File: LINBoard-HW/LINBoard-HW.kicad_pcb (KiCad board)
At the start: 2 copper layers, 77 parts, among them J1 DEBUG, J2 USB_C_Receptacle_USB2.0, SW2 RESET, SW3 BOOT, U1 RP2350_60QFN, U2 TJA1029T, U3 TPS56339DDC, U4 LD1117S33CTR, U5 W25Q128JVS, U6 MCP25625x-x-ML, Y1 ABM8-272-T3

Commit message: board layout started
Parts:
- removed C18: 1uF, Capacitor_SMD:C_0603_1608Metric
- added D1: PESD1LIN, Diode_SMD:D_SOD-323, F.Cu at (0.00, 3.81)
- added D14: Schottky, Diode_SMD:D_SOD-123, F.Cu at (12.3, 31.0)
- added D2: Schottky, Diode_SMD:D_SOD-123, F.Cu at (0.25, -1.52)
- added D3: Schottky, Diode_SMD:D_SOD-123, F.Cu at (9.91, -4.32)
- added J4: ATM15-6P-BM03, ATM:ATM13-6P, F.Cu at (0.00, -23.3)
- added JP6: MASTER, Jumper:SolderJumper-2_P1.3mm_Bridged_RoundedPad1.0x1.5mm, F.Cu at (0.00, 1.27)
- added L2: 5.6uH, Inductors_SMD:Wuerth_LHMI, F.Cu at (12.4, 1.52)
- added Y2: 16MHz 12pF, Crystal:Crystal_SMD_3225-4Pin_3.2x2.5mm, F.Cu at (-12.3, 7.28)
- C1, C10, C11, C12, C13, C14, C15, C16, C17, C19, C2, C22, C23, C24, C25, C26, C27, C28, C29, C3, C30, C31, C4, C5, C6, C7, C8, C9: footprint Capacitor_SMD:C_0603_1608Metric -> Capacitor_SMD:C_0402_1005Metric
- C20, C21: footprint Capacitor_SMD:C_0603_1608Metric -> RP2350_60QFN_minimal:C_0402_1005Metric_small_pads
- D5, D6, D8, D9: footprint LED_SMD:LED_0805_2012Metric -> LED_SMD:LED_0603_1608Metric
- R1, R10, R11, R12, R13, R14, R15, R16, R17, R18, R19, R2, R20, R21, R22, R23, R24, R3, R4, R5, R6, R7, R8, R9: footprint Resistor_SMD:R_0603_1608Metric -> Resistor_SMD:R_0402_1005Metric
- SW2, SW3: footprint Button_Switch_SMD:SW_Push_1P1T_NO_Vertical_Wuerth_434133025816 -> Buttons:TS-1088-AR02016
- moved D5 51.0 mm to (-8.38, 38.4), turned to 180 degrees
- moved U6 50.4 mm to (-10.1, 15.1), turned to 90 degrees
- moved C31 48.6 mm to (-11.7, -5.08)
- moved R1 48.5 mm to (2.29, 1.27), turned to -90 degrees
- moved R4 48.5 mm to (-14.5, 18.8), turned to 90 degrees
- moved C30 47.9 mm to (-15.5, -5.08), turned to 180 degrees
- moved D6 47.7 mm to (-7.11, -3.84), turned to -90 degrees
- moved C2 47.5 mm to (-2.54, 4.83), turned to 90 degrees
- moved U2 47.3 mm to (-0.51, 10.2), turned to 90 degrees
- moved R2 47.3 mm to (-4.06, 11.9), turned to -90 degrees
- moved C5 46.6 mm to (-13.5, 9.91), turned to 180 degrees
- moved U4 46.1 mm to (-12.2, 0.00), turned to 180 degrees
- moved D8 45.7 mm to (-3.81, 38.4)
- moved R18 45.3 mm to (-11.9, 19.6)
- moved R24 45.1 mm to (-7.11, -1.52)
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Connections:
- net Net-(U3-SW) renamed /Power/SW
- C24 pad 1: Net-(D3-K) -> +12P
- C25 pad 1: Net-(D3-K) -> +12P
- C26 pad 1: Net-(D3-K) -> +12P
- J1 pad MP: (no net) -> GND
- R2 pad 1: +12P -> +3.3V
- U1 pad 13: /Connectors/ENABLE -> unconnected-(U1-GPIO9-Pad13)
- U3 pad 3: Net-(D3-K) -> +12P
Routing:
- net +5V: track 0.00 -> 65.7 mm, vias 0 -> 7
- net +3.3V: track 0.00 -> 59.8 mm, vias 0 -> 13
- net CAN_H: track 0.00 -> 33.6 mm
- net CAN_L: track 0.00 -> 26.9 mm
- net GND: track 0.00 -> 24.5 mm, vias 0 -> 22
- net /Microcontroller/QSPI_SS: track 0.00 -> 24.5 mm
- net +12P: track 0.00 -> 23.1 mm
- net +1V1: track 0.00 -> 22.7 mm, vias 0 -> 9
- net /CAN/~{INT}: track 0.00 -> 22.3 mm, vias 0 -> 2
- net /CAN/~{RX0BF}: track 0.00 -> 22.2 mm, vias 0 -> 2
- net /CAN/SCK: track 0.00 -> 17.3 mm, vias 0 -> 2
- net /Microcontroller/QSPI_SD1: track 0.00 -> 16.5 mm
- net /Microcontroller/RUN: track 0.00 -> 16.4 mm
- net /LIN/RX: track 0.00 -> 15.6 mm
- net /CAN/MOSI: track 0.00 -> 15.6 mm, vias 0 -> 2
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- added copper zone on F.Cu, net +12P
- added copper zone on F.Cu, net +12V
- added copper zone on F.Cu, net +1V1
- added copper zone on F.Cu, net +3.3V
- added copper zone on In1.Cu, net +3.3V
- added copper zone on F.Cu, net +5V
- added copper zone on F.Cu, net /Microcontroller/VREG_LX
- added copper zone on F.Cu, net /Power/SW
- added copper zone on B.Cu, net GND
- added copper zone on F.Cu, net GND
- added copper zone on In2.Cu, net GND
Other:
- board outline added: 34.4 x 68.5 mm
- copper layers 2 -> 4
- board text added: "BOOT"
- board text added: "CAN"
- board text added: "LIN"
- board text added: "RUN"
- board text added: "STS"

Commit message: moving some things around
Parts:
- moved D14 4.04 mm to (15.2, 28.2), turned to -90 degrees
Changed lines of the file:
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@@
 	(footprint "Diode_SMD:D_SOD-123"
 		(layer "F.Cu")
-		(at 12.318 30.988 180)
+		(at 15.24 28.194 -90)
 		(descr "SOD-123")
 		(tags "SOD-123")
 		(property "Reference" "D14"
-			(at -74.646 -30.194 0)
+			(at -74.646 -30.194 90)
 			(layer "F.SilkS")
 			(hide yes)
@@
 		)
 		(property "Value" "Schottky"
-			(at 0 2.1 0)
+			(at 0 2.1 90)
 			(layer "F.Fab")
 			(effects
@@
 		)
 		(property "Datasheet" "~"
-			(at 0 0 180)
+			(at 0 0 270)
 			(unlocked yes)
 			(layer "F.Fab")
@@
 		)
 		(property "Description" "Schottky diode, small symbol, filled shape"
-			(at 0 0 180)
+			(at 0 0 270)
 			(unlocked yes)
 			(layer "F.Fab")
@@
 		(fp_line
 			(start -2.36 -1)
-			(end 1.65 -1)
+			(end -2.36 1)
 			(stroke
 				(width 0.12)
@@
 		(fp_line
 			(start -2.36 -1)
-			(end -2.36 1)
+			(end 1.65 -1)
 			(stroke
 				(width 0.12)
@@
 		)
 		(fp_line
-			(start 2.35 -1.15)
-			(end 2.35 1.15)
+			(start -2.35 -1.15)
+			(end -2.35 1.15)
 			(stroke
 				(width 0.05)
@@
 		)
 		(fp_line
-			(start -2.35 -1.15)
-			(end -2.35 1.15)
+			(start 2.35 -1.15)
+			(end 2.35 1.15)
 			(stroke
 				(width 0.05)
@@
 		)
 		(fp_line
-			(start 1.4 0.9)
-			(end -1.4 0.9)
+			(start -1.4 0.9)
+			(end -1.4 -0.9)
 			(stroke
 				(width 0.1)
@@
 		)
 		(fp_line
-			(start 1.4 -0.9)
-			(end 1.4 0.9)
+			(start 1.4 0.9)
+			(end -1.4 0.9)
 			(stroke
 				(width 0.1)
@@
 		)
 		(fp_line
-			(start 0.25 0)
-			(end 0.75 0)
+			(start -0.75 0)
+			(end -0.35 0)
 			(stroke
 				(width 0.1)
@@
 		)
 		(fp_line
-			(start 0.25 -0.4)
-			(end 0.25 0.4)
+			(start -0.35 0)
+			(end -0.35 0.55)
 			(stroke
 				(width 0.1)
@@
 		(fp_line
 			(start -0.35 0)
-			(end -0.35 0.55)
+			(end -0.35 -0.55)
 			(stroke
 				(width 0.1)
@@
 		)
 		(fp_line
-			(start -0.35 0)
-			(end -0.35 -0.55)
+			(start 0.25 0)
+			(end 0.75 0)
 			(stroke
 				(width 0.1)
@@
 		)
 		(fp_line
-			(start -0.75 0)
-			(end -0.35 0)
+			(start 0.25 -0.4)
+			(end 0.25 0.4)
 			(stroke
 				(width 0.1)
@@
 		)
 		(fp_line
-			(start -1.4 0.9)
-			(end -1.4 -0.9)
+			(start -1.4 -0.9)
+			(end 1.4 -0.9)
 			(stroke
 				(width 0.1)
@@
 		)
 		(fp_line
-			(start -1.4 -0.9)
-			(end 1.4 -0.9)
+			(start 1.4 -0.9)
+			(end 1.4 0.9)
 			(stroke
 				(width 0.1)
@@
 		)
 		(fp_text user "${REFERENCE}"
-			(at 0 -2 0)
+			(at 0 -2 90)
 			(layer "F.Fab")
 			(effects
@@
 		)
 		(pad "1" smd roundrect
-			(at -1.65 0 180)
+			(at -1.65 0 270)
 			(size 0.9 1.2)
 			(layers "F.Cu" "F.Mask" "F.Paste")
@@
 		)
 		(pad "2" smd roundrect
-			(at 1.65 0 180)
+			(at 1.65 0 270)
 			(size 0.9 1.2)
 			(layers "F.Cu" "F.Mask" "F.Paste")
@@
 	)
 	(segment
-		(start -14.506 -3.15)
-		(end -14.506 4.302)
+		(start -13.728 5.08)
+		(end -10.414 5.08)
 		(width 0.15)
 		(layer "F.Cu")
@@
 	)
 	(segment
-		(start -14.506 4.302)
-		(end -13.728 5.08)
+		(start -14.506 -3.15)
+		(end -14.506 4.302)
 		(width 0.15)
 		(layer "F.Cu")
@@
 	)
 	(segment
-		(start -11.071906 5.08)
-		(end -9.652 6.499906)
+		(start -10.414 5.08)
+		(end -9.652 5.842)
 		(width 0.15)
 		(layer "F.Cu")
@@
 	)
 	(segment
-		(start -9.172 9.116)
+		(start -8.636 9.670001)
 		(end -8.636 9.116)
 		(width 0.15)
@@
 	)
 	(segment
-		(start -8.636 9.670001)
-		(end -8.636 9.116)
+		(start -10.706 12.2525)
+		(end -10.706 11.740001)
 		(width 0.15)
 		(layer "F.Cu")
@@
 	)
 	(segment
-		(start -9.652 6.499906)
-		(end -9.652 8.636)
+		(start -9.172 9.116)
+		(end -8.636 9.116)
 		(width 0.15)
 		(layer "F.Cu")
@@
 	)
 	(segment
-		(start -10.706 12.2525)
-		(end -10.706 11.740001)
-		(width 0.15)
+		(start -14.506 -5.56)
+		(end -14.478 -5.588)
+		(width 1.5)
 		(layer "F.Cu")
 		(net 4)
 	)
 	(segment
-		(start -14.506 -5.56)
-		(end -14.478 -5.588)
+		(start -14.506 -3.15)
+		(end -14.506 -5.56)
 		(width 1.5)
 		(layer "F.Cu")
@@
 	)
 	(segment
-		(start -13.728 5.08)
-		(end -11.071906 5.08)
+		(start -9.652 5.842)
+		(end -9.652 8.636)
 		(width 0.15)
 		(layer "F.Cu")
@@
 	)
 	(segment
-		(start -14.506 -3.15)
-		(end -14.506 -5.56)
-		(width 1.5)
+		(start -14.506 4.302)
+		(end -13.728 5.08)
+		(width 0.15)
 		(layer "F.Cu")
 		(net 4)

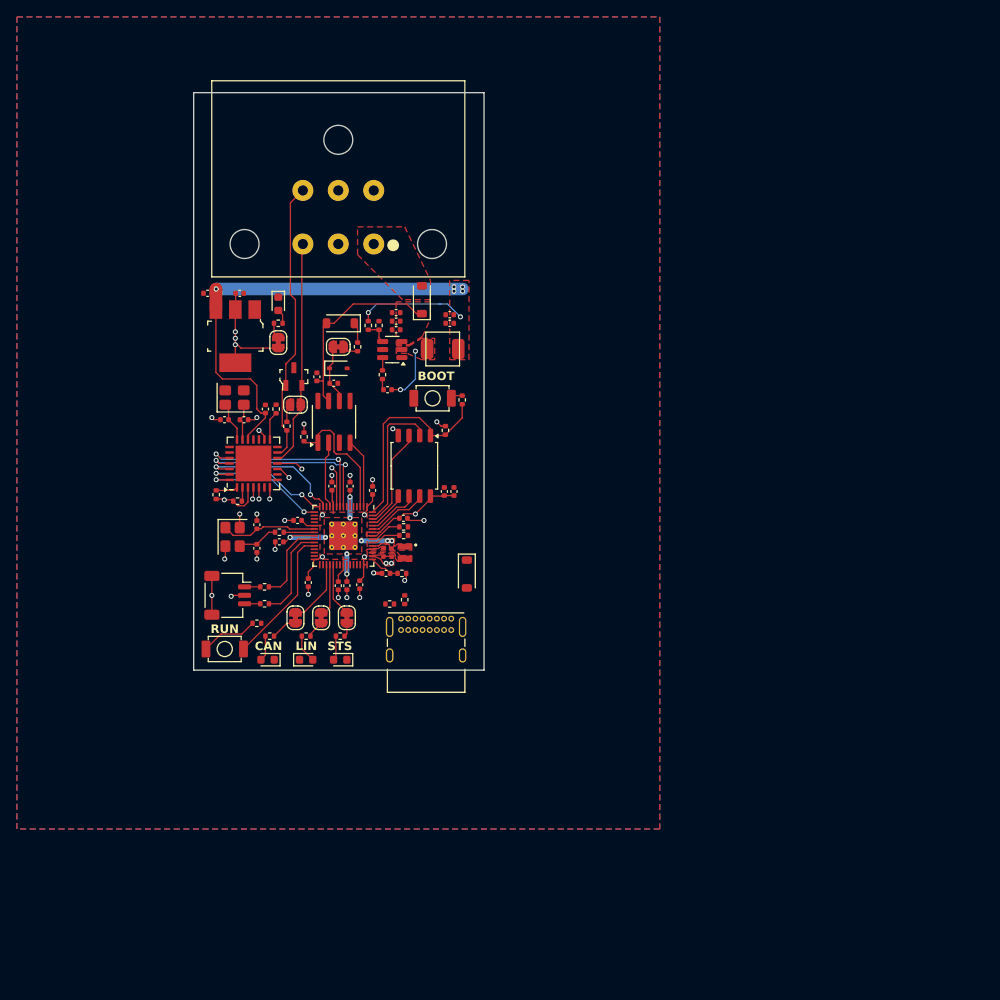
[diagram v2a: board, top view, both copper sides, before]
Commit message: change usb
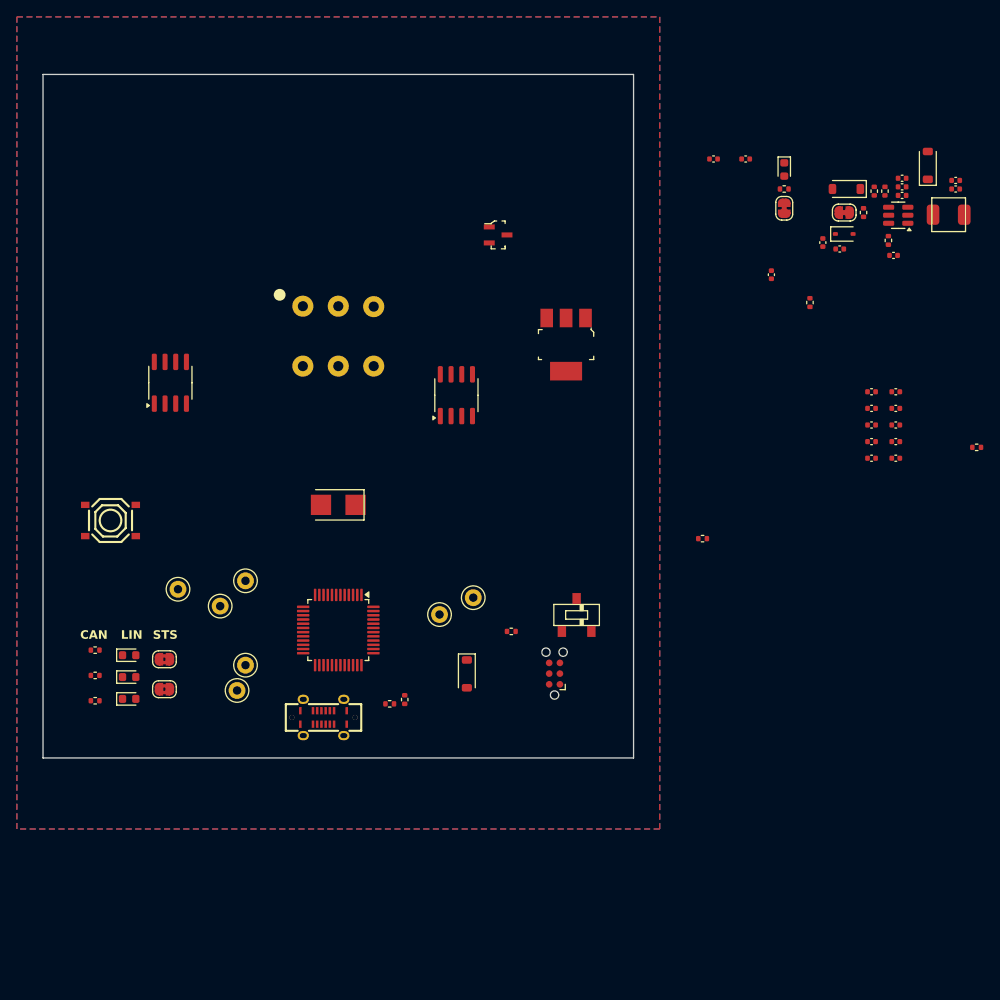
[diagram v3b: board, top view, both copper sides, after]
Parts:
- removed C16, C17, C19: 100nF, Capacitor_SMD:C_0402_1005Metric
- removed C20, C21: 4.7uF, RP2350_60QFN_minimal:C_0402_1005Metric_small_pads
- removed C22: 4.7uF, Capacitor_SMD:C_0402_1005Metric
- removed C23: 2.2uF, Capacitor_SMD:C_0402_1005Metric
- removed C5: 22pF, Capacitor_SMD:C_0402_1005Metric
- removed C6: 15pF, Capacitor_SMD:C_0402_1005Metric
- removed D9: CAN, LED_SMD:LED_0603_1608Metric
- removed JP3: CAN_LED, Jumper:SolderJumper-2_P1.3mm_Bridged_RoundedPad1.0x1.5mm
- removed JP4: STATUS_LED, Jumper:SolderJumper-2_P1.3mm_Bridged_RoundedPad1.0x1.5mm
- removed L1: 3.3uH, RP2350_60QFN_minimal:L_pol_2016
- removed R10, R18, R19: 10K, Resistor_SMD:R_0402_1005Metric
- removed R11, R12: 1K, Resistor_SMD:R_0402_1005Metric
- removed R15, R16: 100R, Resistor_SMD:R_0402_1005Metric
- removed R17, R20, R8: 120R, Resistor_SMD:R_0402_1005Metric
- removed R9: 27R, Resistor_SMD:R_0402_1005Metric
- removed SW3: BOOT, Buttons:TS-1088-AR02016
- removed U5: W25Q128JVS, Package_SO:SOIC-8_5.3x5.3mm_P1.27mm
- removed Y2: 16MHz 12pF, Crystal:Crystal_SMD_3225-4Pin_3.2x2.5mm
- added D7: LIN, LED_SMD:LED_0603_1608Metric, F.Cu at (-24.8, 40.4)
- added FB1: FerriteBead_Small, Resistor_SMD:R_0402_1005Metric, F.Cu at (43.2, 24.0)
- added SW1: BOOT, SlideSwitch:CJS-1200TB, F.Cu at (28.2, 33.0)
- added TP1: E_UART3_TX, TestPoint:TestPoint_Keystone_5000-5004_Miniature, F.Cu at (-11.0, 39.0)
- added TP2: E_UART3_RX, TestPoint:TestPoint_Keystone_5000-5004_Miniature, F.Cu at (-12.0, 42.0)
- added TP3: E_I2C1_SCL, TestPoint:TestPoint_Keystone_5000-5004_Miniature, F.Cu at (16.0, 31.0)
- added TP4: E_I2C1_SDA, TestPoint:TestPoint_Keystone_5000-5004_Miniature, F.Cu at (12.0, 33.0)
- added TP5: E1, TestPoint:TestPoint_Keystone_5000-5004_Miniature, F.Cu at (-11.0, 29.0)
- added TP6: E2, TestPoint:TestPoint_Keystone_5000-5004_Miniature, F.Cu at (-14.0, 32.0)
- added TP7: E3, TestPoint:TestPoint_Keystone_5000-5004_Miniature, F.Cu at (-19.0, 30.0)
- C13: value 100nF -> 4.7uF
- C15: value 100nF -> 1uF
- C4: value 22pF -> 100nF
- C7: value 15pF -> 27pF
- C8: value 100nF -> 27pF
- C9: value 4.7uF -> 100nF
- D5: value STATUS -> CAN
- D8: value LIN -> Status
- J1: value DEBUG -> TC; footprint Connector_JST:JST_SH_SM03B-SRSS-TB_1x03-1MP_P1.00mm_Horizontal -> Connector:Tag-Connect_TC2030-IDC-NL_2x03_P1.27mm_Vertical
- J2: value USB_C_Receptacle_USB2.0 -> TYPE-C 16PLT-H10.0; footprint Connector_USB:USB_C_Receptacle_GCT_USB4085 -> vert_usb:TYPE-C-SMD_USB4120-03-C
- J4: footprint ATM:ATM13-6P -> ATM:ATM15-6P_NoMountingHoles
- JP1: value TERM -> CYA; footprint Jumper:SolderJumper-2_P1.3mm_Open_RoundedPad1.0x1.5mm -> Jumper:SolderJumper-2_P1.3mm_Bridged2Bar_RoundedPad1.0x1.5mm
- JP2: value LIN_LED -> CYA; footprint Jumper:SolderJumper-2_P1.3mm_Bridged_RoundedPad1.0x1.5mm -> Jumper:SolderJumper-2_P1.3mm_Bridged2Bar_RoundedPad1.0x1.5mm
- R3: value 1K -> 10K
- R4: value 10K -> 1K
- R5: value 27R -> 10K
- R6: value 33R -> 10K
- R7: value 120R -> 10K
- SW2: footprint Buttons:TS-1088-AR02016 -> switch_pb:SW-SMD_4P-L5.1-W5.1-P3.70-LS6.5-TL_H1.5
- U1: value RP2350_60QFN -> PCA82C250; footprint RP2350_60QFN_minimal:RP2350-QFN-60-1EP_7x7_P0.4mm_EP3.4x3.4mm_ThermalVias -> Package_SO:SOIC-8_3.9x4.9mm_P1.27mm
- U6: value MCP25625x-x-ML -> STM32F302C8Tx; footprint Package_DFN_QFN:QFN-28-1EP_6x6mm_P0.65mm_EP4.25x4.25mm -> Package_QFP:LQFP-48_7x7mm_P0.5mm
- Y1: value ABM8-272-T3 -> 8mHz; footprint Crystal:Crystal_SMD_3225-4Pin_3.2x2.5mm -> Crystals_Modify:Crystal_SMD_5032-2Pin_5.0x3.2mm_HandSoldering
- moved R4 90.3 mm to (75.7, 13.2), turned to 0 degrees
- moved C7 74.7 mm to (63.2, 8.56), turned to 0 degrees
- moved C4 74.5 mm to (63.2, 6.59)
- moved C13 72.1 mm to (66.1, 10.5), turned to 0 degrees
- moved C9 71.2 mm to (63.2, 12.5)
- moved C14 68.3 mm to (66.1, 12.5), turned to 0 degrees
- moved C12 66.9 mm to (66.1, 8.56), turned to 0 degrees
- moved C8 65.0 mm to (63.2, 10.5), turned to 0 degrees
- moved C15 62.1 mm to (66.1, 14.5), turned to 0 degrees
- moved C1 62.1 mm to (59.4, -10.3)
- moved C27 62.1 mm to (65.8, -9.57)
- moved C28 62.1 mm to (73.2, -18.5)
- moved C29 62.1 mm to (73.2, -17.4)
- moved C3 62.1 mm to (51.3, -7.28)
- moved D2 62.1 mm to (60.2, -17.4)
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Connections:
- net Net-(D14-A) renamed /Connectors/VBUS
- C10 pad 1: GND -> +3V3
- C10 pad 2: +1V1 -> GND
- C11 pad 1: GND -> +3V3
- C11 pad 2: +3.3V -> GND
- C12 pad 1: GND -> +3V3
- C12 pad 2: +3.3V -> GND
- C13 pad 1: GND -> +3V3
- C13 pad 2: +3.3V -> GND
- C14 pad 1: GND -> +3V3
- C14 pad 2: +3.3V -> GND
- C15 pad 1: GND -> +3V3
- C15 pad 2: +3.3V -> GND
- C4 pad 1: Net-(U6-OSC2) -> GND
- C4 pad 2: GND -> /Microcontroller/NRST
- C7 pad 1: Net-(C7-Pad1) -> Net-(U6-PF0)
- C8 pad 2: +1V1 -> Net-(U6-PF1)
- C9 pad 1: GND -> +3V3
- C9 pad 2: +1V1 -> GND
- J1 pad 1: /Microcontroller/SWCLK -> +3V3
- J1 pad 2: GND -> /Microcontroller/SWDIO
- J1 pad 3: /Microcontroller/SWD -> /Microcontroller/NRST
- JP1 pad 1: CAN_L -> Net-(JP1-A)
- JP1 pad 2: Net-(JP1-B) -> /Microcontroller/UART2_TX
- JP2 pad 2: Net-(JP2-B) -> /Microcontroller/UART2_RX
- R13 pad 1: Net-(J2-CC2) -> Net-(J2-CC1)
- R14 pad 1: Net-(J2-CC1) -> Net-(J2-CC2)
- R3 pad 1: /Microcontroller/XOUT -> Net-(U6-BOOT0)
- R3 pad 2: Net-(C7-Pad1) -> Net-(SW1-B)
- R4 pad 1: +3.3V -> +3V3
- R4 pad 2: Net-(U6-~{CS}) -> /CAN/TX
- R5 pad 1: /Connectors/USB_D- -> Net-(U6-PB0)
- R5 pad 2: Net-(U1-USB_DM) -> Net-(D5-A)
- R6 pad 1: +3.3V -> Net-(U6-PB1)
- R6 pad 2: /Microcontroller/VREG_AVDD -> Net-(D7-A)
- R7 pad 1: Net-(JP2-A) -> Net-(U6-PB2)
- SW2 pad 1: Net-(R11-Pad1) -> GND
- SW2 pad 2: /Microcontroller/RUN -> /Microcontroller/NRST
- U1 pad 1: +3.3V -> /CAN/TX
- U1 pad 2: /LIN/TX -> GND
- U1 pad 3: /LIN/RX -> +5V
- U1 pad 4: unconnected-(U1-GPIO2-Pad4) -> /CAN/RX
- U1 pad 5: unconnected-(U1-GPIO3-Pad5) -> +3V3
- U1 pad 6: +1V1 -> CAN_L
- U1 pad 7: unconnected-(U1-GPIO4-Pad7) -> CAN_H
- U1 pad 8: /CAN/~{INT} -> /CAN/STANDBY
- U6 pad 1: Net-(U6-~{CS}) -> +3V3
- U6 pad 10: Net-(U6-R_{XD}) -> unconnected-(U6-PA0-Pad10)
- U6 pad 11: +3.3V -> /LIN/~{SLP}
- U6 pad 12: CAN_L -> Net-(JP1-A)
- U6 pad 13: CAN_H -> Net-(JP2-A)
- U6 pad 16: Net-(U6-T_{XD}) -> Net-(U6-PA6)
- U6 pad 17: unconnected-(U6-NC-Pad17) -> Net-(U6-PA7)
- U6 pad 18: GND -> Net-(U6-PB0)
- U6 pad 19: +5V -> Net-(U6-PB1)
- U6 pad 2: Net-(U6-~{RESET}) -> /CAN/STANDBY
- U6 pad 20: Net-(U6-OSC2) -> Net-(U6-PB2)
- U6 pad 22: GND -> Net-(U6-PB11)
- U6 pad 23: unconnected-(U6-~{Rx1BF}-Pad23) -> GND
- U6 pad 24: /CAN/~{RX0BF} -> +3V3
- U6 pad 25: /CAN/~{INT} -> unconnected-(U6-PB12-Pad25)
- U6 pad 26: /CAN/SCK -> unconnected-(U6-PB13-Pad26)
- U6 pad 27: /CAN/MOSI -> unconnected-(U6-PB14-Pad27)
- U6 pad 28: /CAN/MISO -> unconnected-(U6-PB15-Pad28)
- U6 pad 29: GND -> unconnected-(U6-PA8-Pad29)
- U6 pad 3: +3.3V -> unconnected-(U6-PC14-Pad3)
- U6 pad 4: Net-(U6-T_{XD}) -> unconnected-(U6-PC15-Pad4)
- U6 pad 5: Net-(U6-R_{XD}) -> Net-(U6-PF0)
- U6 pad 6: unconnected-(U6-CLKOUT-Pad6) -> Net-(U6-PF1)
- U6 pad 7: /CAN/~{TX0RTS} -> /Microcontroller/NRST
- U6 pad 8: unconnected-(U6-~{Tx1RTS}-Pad8) -> GND
- U6 pad 9: unconnected-(U6-~{Tx2RTS}-Pad9) -> Net-(U6-VDDA)
- Y1 pad 1: /Microcontroller/XIN -> Net-(U6-PF0)
- Y1 pad 2: GND -> Net-(U6-PF1)
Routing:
- net +5V: track 66.1 -> 0.00 mm, vias 7 -> 0
- net +3.3V: track 59.8 -> 0.00 mm, vias 13 -> 0
- net CAN_H: track 33.6 -> 0.00 mm
- net CAN_L: track 26.9 -> 0.00 mm
- net GND: track 24.5 -> 0.00 mm, vias 22 -> 0
- net /Microcontroller/QSPI_SS: track 24.5 -> 0.00 mm
- net +12P: track 23.1 -> 0.00 mm
- net +1V1: track 22.7 -> 0.00 mm, vias 9 -> 0
- net /CAN/~{INT}: track 22.3 -> 0.00 mm, vias 2 -> 0
- net /CAN/~{RX0BF}: track 22.2 -> 0.00 mm, vias 2 -> 0
- net /CAN/SCK: track 17.3 -> 0.00 mm, vias 2 -> 0
- net /Microcontroller/QSPI_SD1: track 16.5 -> 0.00 mm
- net /Microcontroller/RUN: track 16.4 -> 0.00 mm
- net /LIN/RX: track 15.6 -> 0.00 mm
- net /CAN/MOSI: track 15.6 -> 0.00 mm, vias 2 -> 0
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- removed copper zone on F.Cu, net +12P
- removed copper zone on F.Cu, net +12V
- removed copper zone on F.Cu, net +1V1
- removed copper zone on F.Cu, net +3.3V
- removed copper zone on F.Cu, net +5V
- removed copper zone on F.Cu, net /Microcontroller/VREG_LX
- removed copper zone on F.Cu, net /Power/SW
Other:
- board size 34.4 x 68.5 mm -> 70 x 81 mm
- board text removed: "BOOT"
- board text removed: "RUN"

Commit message: back to ra connectors
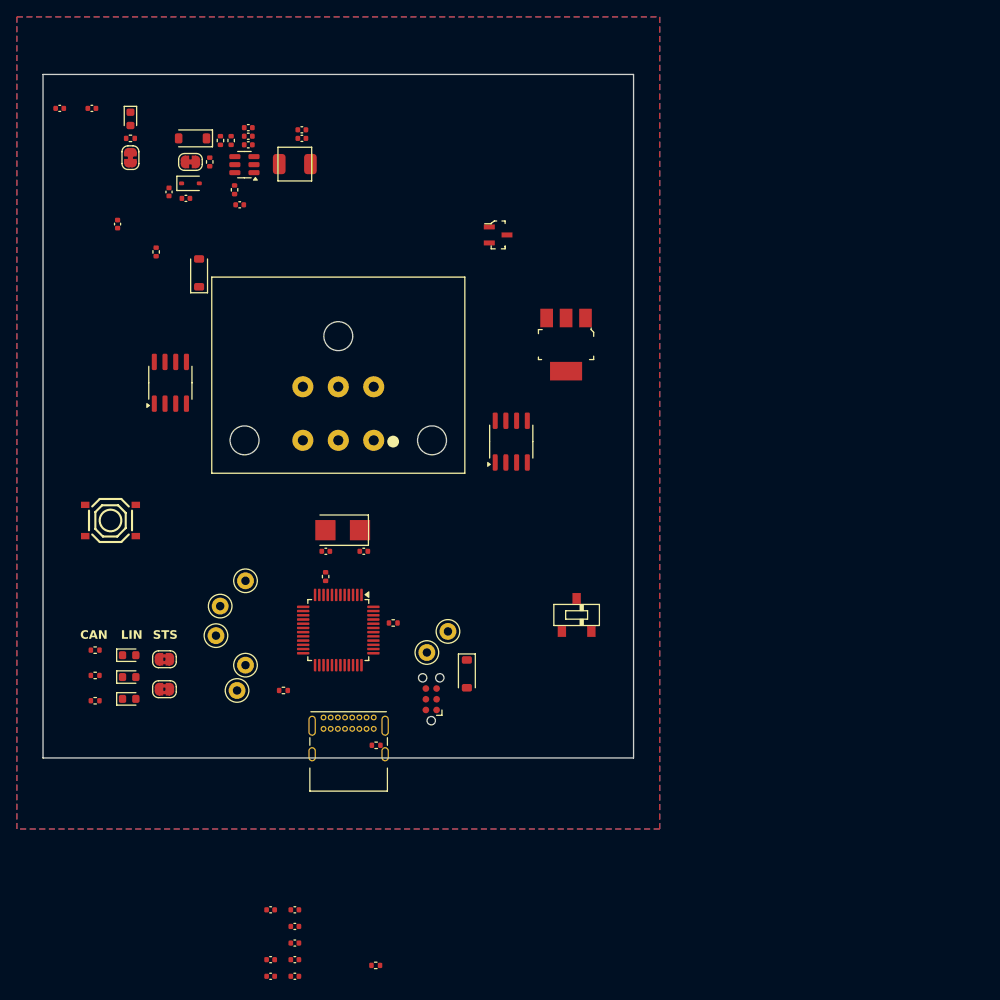
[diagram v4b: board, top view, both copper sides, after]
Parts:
- J2: footprint vert_usb:TYPE-C-SMD_USB4120-03-C -> Connector_USB:USB_C_Receptacle_GCT_USB4085
- J4: footprint ATM:ATM15-6P_NoMountingHoles -> ATM:ATM13-6P
- moved C10 94.0 mm to (-8.02, 75.9)
- moved C11 94.0 mm to (-5.15, 68.0)
- moved C12 94.0 mm to (-5.15, 70.0)
- moved C13 94.0 mm to (-5.15, 71.9)
- moved C14 94.0 mm to (-5.15, 73.9)
- moved C15 94.0 mm to (-5.15, 75.9)
- moved C4 94.0 mm to (-8.02, 68.0)
- moved C9 94.0 mm to (-8.02, 73.9)
- moved R4 94.0 mm to (4.44, 74.6)
- moved D3 87.3 mm to (-16.5, -7.50)
- moved C1 77.7 mm to (-18.1, -16.3)
- moved C2 77.7 mm to (-20.1, -17.1)
- moved C24 77.7 mm to (-10.7, -22.7)
- moved C25 77.7 mm to (-10.7, -23.7)
- moved C26 77.7 mm to (-10.7, -24.7)
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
